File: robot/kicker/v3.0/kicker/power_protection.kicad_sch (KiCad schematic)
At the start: 40 parts, among them Q1 BSS138, Q2 SQJA80EP-T1_GE3, Q3 SQJA80EP-T1_GE3, SW1 SW_Push, U1 LTC4367, U2 LTC2955-1

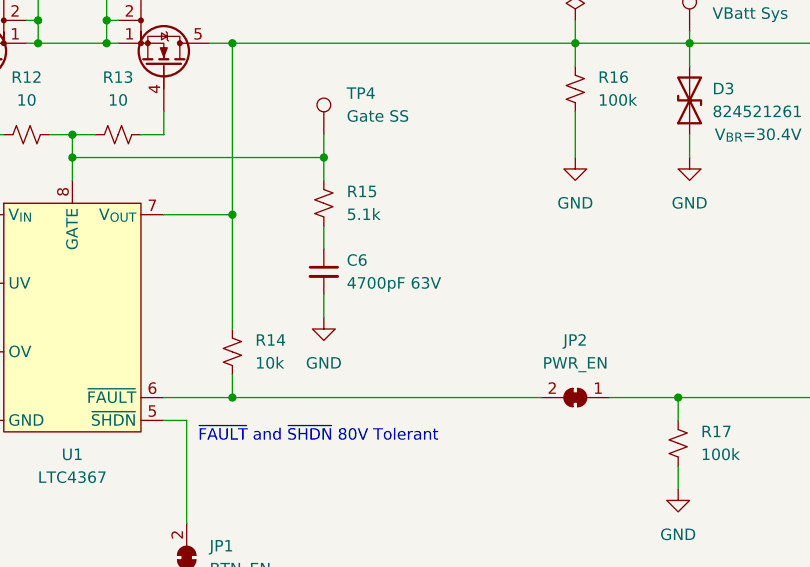
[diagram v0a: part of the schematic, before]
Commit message: kicker v3.0 footprint work
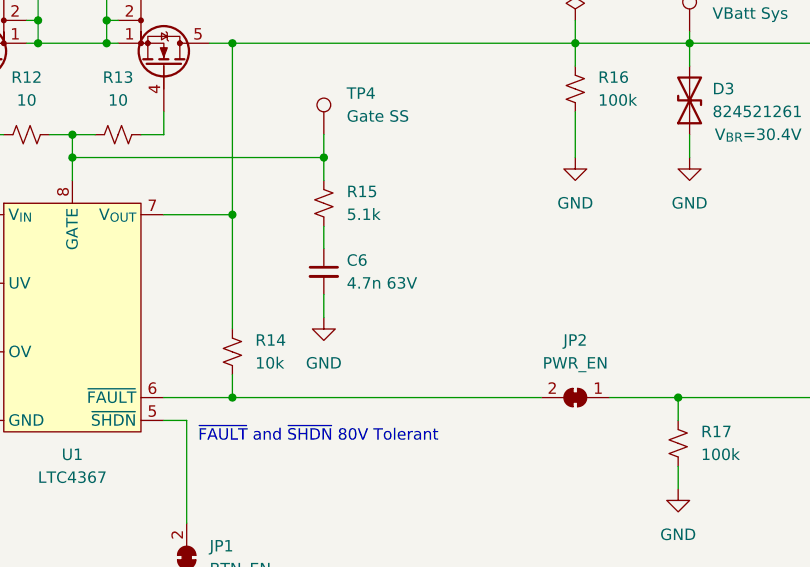
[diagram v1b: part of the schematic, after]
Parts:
- C1, C2: footprint (none) -> Capacitor_SMD:C_1210_3225Metric
- C3, C4, C5: footprint (none) -> Capacitor_SMD:C_0402_1005Metric
- C6: value 4700pF 63V -> 4.7n 63V; footprint (none) -> Capacitor_SMD:C_0402_1005Metric
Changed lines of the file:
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@@
       (effects (font (size 1.27 1.27)) (justify left))
     )
-    (property "Footprint" "" (at 166.37 121.92 0)
+    (property "Footprint" "Capacitor_SMD:C_0402_1005Metric" (at 166.37 121.92 0)
       (effects (font (size 1.27 1.27)) hide)
     )
@@
       (effects (font (size 1.27 1.27)) (justify left))
     )
-    (property "Footprint" "" (at 217.17 148.59 0)
+    (property "Footprint" "Capacitor_SMD:C_0402_1005Metric" (at 217.17 148.59 0)
       (effects (font (size 1.27 1.27)) hide)
     )
@@
       (effects (font (size 1.27 1.27)) (justify left))
     )
-    (property "Footprint" "" (at 256.54 142.24 0)
+    (property "Footprint" "Capacitor_SMD:C_0402_1005Metric" (at 256.54 142.24 0)
       (effects (font (size 1.27 1.27)) hide)
     )
@@
       (effects (font (size 1.27 1.27)) (justify left))
     )
-    (property "Footprint" "" (at 114.3 50.8 0)
+    (property "Footprint" "Capacitor_SMD:C_1210_3225Metric" (at 114.3 50.8 0)
       (effects (font (size 1.27 1.27)) hide)
     )
@@
       (effects (font (size 1.27 1.27)) (justify left))
     )
-    (property "Value" "4700pF 63V" (at 274.32 69.8562 0)
-      (effects (font (size 1.27 1.27)) (justify left))
-    )
-    (property "Footprint" "" (at 271.78 68.58 0)
+    (property "Value" "4.7n 63V" (at 274.32 69.8562 0)
+      (effects (font (size 1.27 1.27)) (justify left))
+    )
+    (property "Footprint" "Capacitor_SMD:C_0402_1005Metric" (at 271.78 68.58 0)
       (effects (font (size 1.27 1.27)) hide)
     )
@@
       (effects (font (size 1.27 1.27)) (justify left))
     )
-    (property "Footprint" "" (at 92.71 59.69 0)
-      (effects (font (size 1.27 1.27)) hide)
-    )
+    (property "Footprint" "Capacitor_SMD:C_1210_3225Metric" (at 92.71 59.69 0)
+      (effects (font (size 1.27 1.27)) hide)
+    )

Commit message: kicker v3.0 footprint work
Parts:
- SW1: value SW_Push -> PWR_ON; footprint (none) -> Button_Switch_SMD:SW_SPST_TL3305A
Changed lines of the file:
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@@
   )
   (polyline (pts (xy 17.78 17.78) (xy 381 17.78))
-    (stroke (width 0) (type dash))
+    (stroke (width 0) (type solid))
   )
   (wire (pts (xy 214.63 69.85) (xy 233.68 69.85))
@@
   )
   (polyline (pts (xy 17.78 212.09) (xy 381 212.09))
-    (stroke (width 0) (type dash))
+    (stroke (width 0) (type solid))
   )
   (wire (pts (xy 312.42 53.34) (xy 312.42 55.88))
@@
   )
   (polyline (pts (xy 381 212.09) (xy 381 17.78))
-    (stroke (width 0) (type dash))
+    (stroke (width 0) (type solid))
   )
   (polyline (pts (xy 17.78 17.78) (xy 17.78 212.09))
-    (stroke (width 0) (type dash))
+    (stroke (width 0) (type solid))
   )
   (wire (pts (xy 271.78 63.5) (xy 271.78 66.04))
@@
       (effects (font (size 1.27 1.27)) (justify right))
     )
-    (property "Value" "SW_Push" (at 201.93 152.4 90)
-      (effects (font (size 1.27 1.27)) (justify right))
-    )
-    (property "Footprint" "" (at 195.58 151.13 0)
-      (effects (font (size 1.27 1.27)) hide)
-    )
+    (property "Value" "PWR_ON" (at 201.93 152.4 90)
+      (effects (font (size 1.27 1.27)) (justify right))
+    )
+    (property "Footprint" "Button_Switch_SMD:SW_SPST_TL3305A" (at 195.58 151.13 0)
+      (effects (font (size 1.27 1.27)) hide)
+    )

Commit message: kicker v3.0 footprint work
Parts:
- U2: footprint (none) -> AT-IC:LTC2955-TS8
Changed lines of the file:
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@@
       (effects (font (size 1.27 1.27)))
     )
-    (property "Footprint" "" (at 243.84 127 0)
+    (property "Footprint" "AT-IC:LTC2955-TS8" (at 243.84 127 0)
       (effects (font (size 1.27 1.27)) hide)
     )

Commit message: component/footprint swaps, layout work
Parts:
- F1: footprint AT-Fuses:3557-2 -> Fuse:Fuse_Littelfuse-NANO2-451_453
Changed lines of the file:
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@@
       (effects (font (size 1.27 1.27)))
     )
-    (property "Footprint" "AT-Fuses:3557-2" (at 53.34 44.958 90)
+    (property "Footprint" "Fuse:Fuse_Littelfuse-NANO2-451_453" (at 53.34 44.958 90)
       (effects (font (size 1.27 1.27)) hide)
     )
-    (property "Datasheet" "~" (at 53.34 43.18 0)
+    (property "Datasheet" "0451015.MRL" (at 53.34 43.18 0)
       (effects (font (size 1.27 1.27)) hide)
     )

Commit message: kicker v3.0 layout work
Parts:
- F1: footprint Fuse:Fuse_Littelfuse-NANO2-451_453 -> AT-Fuses:3557-2
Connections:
- net V_{BATT}_FUSED: now reaches C1.1, C2.1, F1.2, Q2.5 (D), R3.2, R4.2, R6.2, TP1.1
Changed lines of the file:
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@@
+    (effects (font (size 1.27 1.27)) (justify left bottom))
+  )
+  (label "V_{BATT}_FUSED" (at 67.31 43.18 0) (fields_autoplaced)
     (effects (font (size 1.27 1.27)) (justify left bottom))
   )
@@
       (effects (font (size 1.27 1.27)))
     )
-    (property "Footprint" "Fuse:Fuse_Littelfuse-NANO2-451_453" (at 53.34 44.958 90)
-      (effects (font (size 1.27 1.27)) hide)
-    )
+    (property "Footprint" "AT-Fuses:3557-2" (at 53.34 44.958 90)
+      (effects (font (size 1.27 1.27)) hide)
+    )

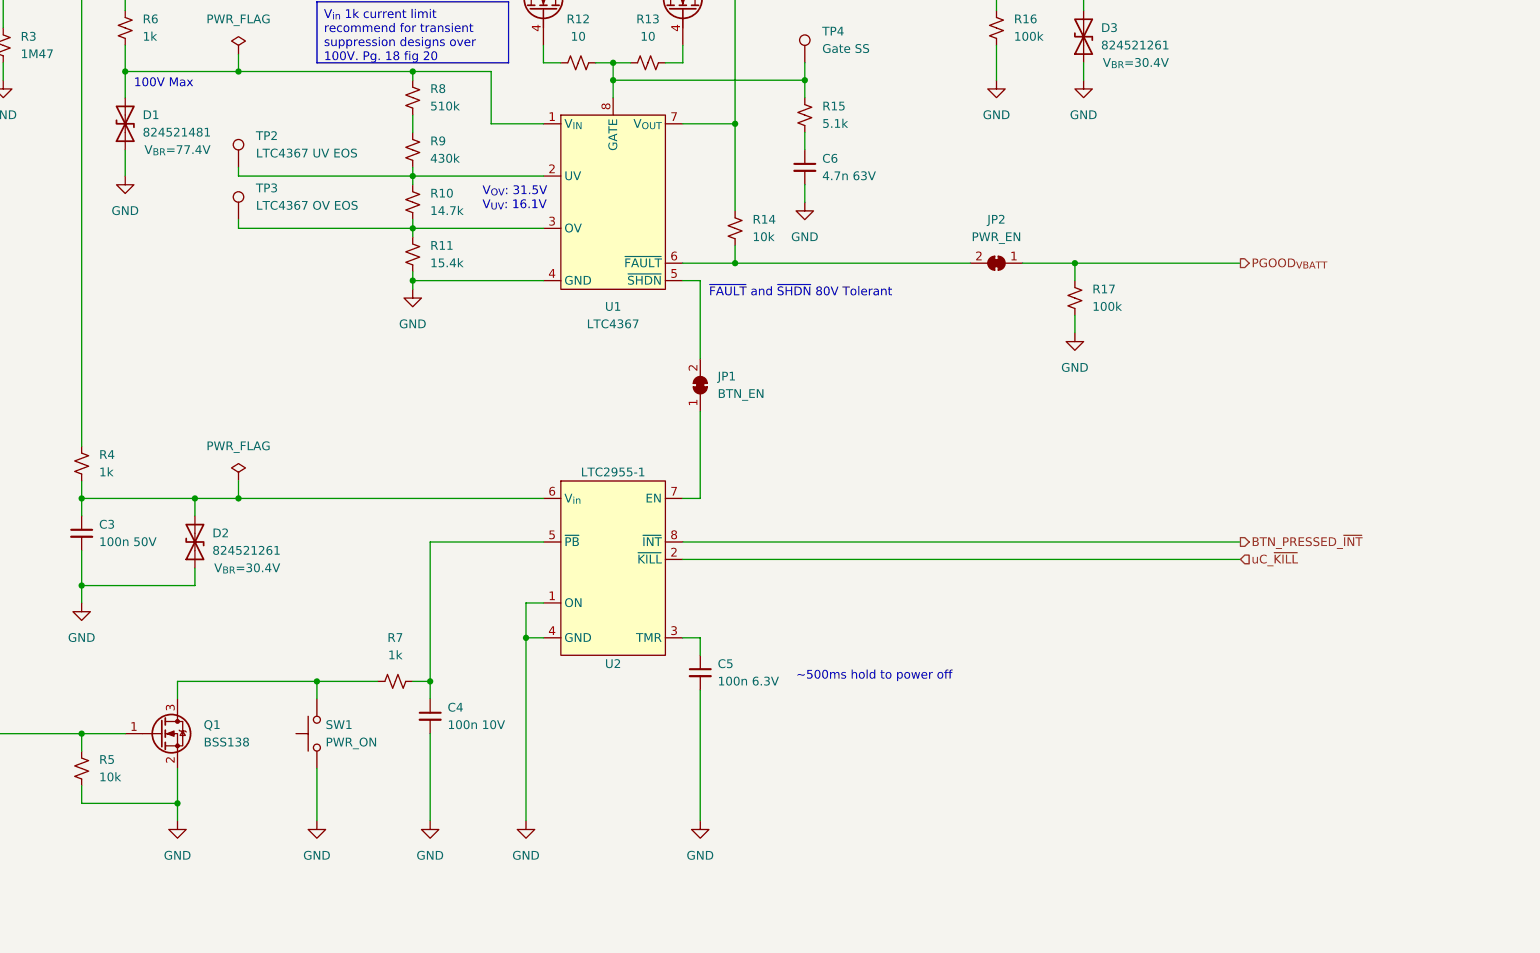
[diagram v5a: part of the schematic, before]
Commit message: kicker v3.0 changes from design review
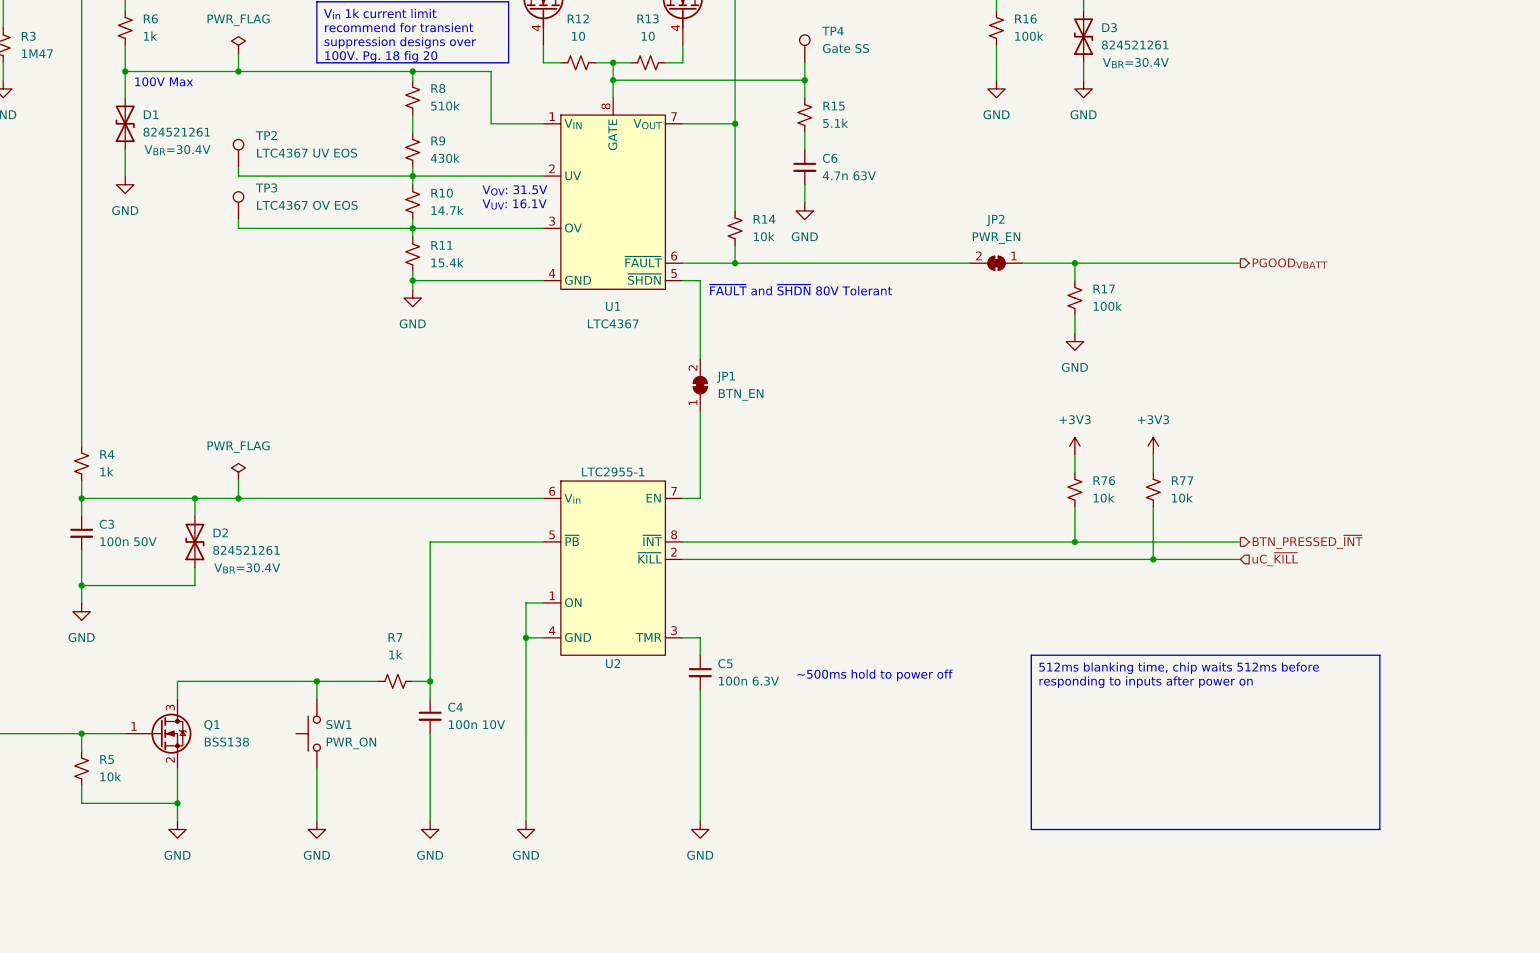
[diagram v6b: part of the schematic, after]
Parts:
- added R76, R77: 10k, Resistor_SMD:R_0402_1005Metric, symbol Device:R_Small_US
- D1: value 824521481 -> 824521261; V_{BR} V_{BR}=77.4V -> V_{BR}=30.4V
- R3: footprint Resistor_SMD:R_0402_1005Metric -> Resistor_SMD:R_0805_2012Metric
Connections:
- net BTN_PRESSED_~{INT}: now also R76.2
- net uC_~{KILL}: now also R77.2
- new net +3V3: R76.1, R77.1

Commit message: finish schematic fixes from the design review, layout work
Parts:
- C4: value 100n 10V -> 100n 50V
- C5: value 100n 6.3V -> 100n 50V
- R3: value 1M47 -> 1.47M
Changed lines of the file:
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@@
       (effects (font (size 1.27 1.27)) (justify right))
     )
-    (property "Value" "1M47" (at 157.48 52.07 0)
+    (property "Value" "1.47M" (at 157.48 52.07 0)
       (effects (font (size 1.27 1.27)) (justify right))
     )
@@
       (effects (font (size 1.27 1.27)) (justify left))
     )
-    (property "Value" "100n 10V" (at 219.71 149.8662 0)
+    (property "Value" "100n 50V" (at 219.71 149.8662 0)
       (effects (font (size 1.27 1.27)) (justify left))
     )
@@
       (effects (font (size 1.27 1.27)) (justify left))
     )
-    (property "Value" "100n 6.3V" (at 259.08 143.5162 0)
-      (effects (font (size 1.27 1.27)) (justify left))
-    )
+    (property "Value" "100n 50V" (at 259.08 143.5162 0)
+      (effects (font (size 1.27 1.27)) (justify left))
+    )

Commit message: layout work
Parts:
- TP1, TP2, TP3, TP4, TP5: footprint TestPoint:TestPoint_Pad_D1.5mm -> TestPoint:TestPoint_Pad_D1.0mm
- renumbered R76 to R18, R77 to R19
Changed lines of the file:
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@@
       (effects (font (size 1.27 1.27)) (justify left))
     )
-    (property "Footprint" "TestPoint:TestPoint_Pad_D1.5mm" (at 317.5 41.91 0)
+    (property "Footprint" "TestPoint:TestPoint_Pad_D1.0mm" (at 317.5 41.91 0)
       (effects (font (size 1.27 1.27)) hide)
     )
@@
         )
         (path "/7c007fad-bfbf-4e78-a837-1f8089552516/966fab5a-ccd3-4169-a651-1134c1c683b9"
-          (reference "#PWR0143") (unit 1)
+          (reference "#PWR023") (unit 1)
         )
       )
@@
       (effects (font (size 1.27 1.27)) (justify left))
     )
-    (property "Footprint" "TestPoint:TestPoint_Pad_D1.5mm" (at 194.31 68.58 0)
+    (property "Footprint" "TestPoint:TestPoint_Pad_D1.0mm" (at 194.31 68.58 0)
       (effects (font (size 1.27 1.27)) hide)
     )
@@
   (symbol (lib_id "Device:R_Small_US") (at 311.15 115.57 0) (unit 1)
     (in_bom yes) (on_board yes) (dnp no) (fields_autoplaced)
-    (property "Reference" "R76" (at 313.69 114.3 0)
+    (property "Reference" "R18" (at 313.69 114.3 0)
       (effects (font (size 1.27 1.27)) (justify left))
     )
@@
       (project "kicker"
         (path "/7c007fad-bfbf-4e78-a837-1f8089552516/966fab5a-ccd3-4169-a651-1134c1c683b9"
-          (reference "R76") (unit 1)
+          (reference "R18") (unit 1)
         )
       )
@@
   (symbol (lib_id "Device:R_Small_US") (at 322.58 115.57 0) (unit 1)
     (in_bom yes) (on_board yes) (dnp no) (fields_autoplaced)
-    (property "Reference" "R77" (at 325.12 114.3 0)
+    (property "Reference" "R19" (at 325.12 114.3 0)
       (effects (font (size 1.27 1.27)) (justify left))
     )
@@
       (project "kicker"
         (path "/7c007fad-bfbf-4e78-a837-1f8089552516/966fab5a-ccd3-4169-a651-1134c1c683b9"
-          (reference "R77") (unit 1)
+          (reference "R19") (unit 1)
         )
       )
@@
       (effects (font (size 1.27 1.27)) (justify left))
     )
-    (property "Footprint" "TestPoint:TestPoint_Pad_D1.5mm" (at 97.79 40.64 0)
+    (property "Footprint" "TestPoint:TestPoint_Pad_D1.0mm" (at 97.79 40.64 0)
       (effects (font (size 1.27 1.27)) hide)
     )
@@
       (effects (font (size 1.27 1.27)) (justify left))
     )
-    (property "Footprint" "TestPoint:TestPoint_Pad_D1.5mm" (at 276.86 53.34 0)
+    (property "Footprint" "TestPoint:TestPoint_Pad_D1.0mm" (at 276.86 53.34 0)
       (effects (font (size 1.27 1.27)) hide)
     )
@@
   (symbol (lib_id "power:GND") (at 312.42 55.88 0) (unit 1)
     (in_bom yes) (on_board yes) (dnp no) (fields_autoplaced)
-    (property "Reference" "#PWR023" (at 312.42 62.23 0)
+    (property "Reference" "#PWR024" (at 312.42 62.23 0)
       (effects (font (size 1.27 1.27)) hide)
     )
@@
       (project "kicker"
         (path "/7c007fad-bfbf-4e78-a837-1f8089552516/966fab5a-ccd3-4169-a651-1134c1c683b9"
-          (reference "#PWR023") (unit 1)
+          (reference "#PWR024") (unit 1)
         )
       )
@@
       (effects (font (size 1.27 1.27)) (justify left))
     )
-    (property "Footprint" "TestPoint:TestPoint_Pad_D1.5mm" (at 194.31 76.2 0)
+    (property "Footprint" "TestPoint:TestPoint_Pad_D1.0mm" (at 194.31 76.2 0)
       (effects (font (size 1.27 1.27)) hide)
     )
@@
         )
         (path "/7c007fad-bfbf-4e78-a837-1f8089552516/966fab5a-ccd3-4169-a651-1134c1c683b9"
-          (reference "#PWR0144") (unit 1)
-        )
-      )
+          (reference "#PWR025") (unit 1)
+        )
+      )
